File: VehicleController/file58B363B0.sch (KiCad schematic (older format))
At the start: 4 parts

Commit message: Added GPS, DAC, Isolation sheet, buzzer to VC
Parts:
- added C?: C_Small, symbol C_Small
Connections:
- wire segments 23 -> 27
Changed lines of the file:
@@
 $Descr A4 11693 8268
 encoding utf-8
-Sheet 4 4
+Sheet 4 5
 Title ""
 Date ""
@@
 	6900 3150 7050 3150
 Wire Wire Line
-	7050 3150 7050 3350
+	7050 3150 7050 3250
+Wire Wire Line
+	7050 3250 7050 3350
 Wire Wire Line
 	6900 3250 7050 3250
 Wire Wire Line
-	6250 2900 6250 3050
+	6250 2900 6250 2950
+Wire Wire Line
+	6250 2950 6250 3050
 Wire Wire Line
 	6400 2950 6250 2950
@@
 Text Label 7200 3050 2    60   ~ 0
 CANL
+$Comp
+L C_Small C?
+U 1 1 58B0DDAC
+P 5250 3950
+F 0 "C?" H 5342 3996 50  0000 L CNN
+F 1 "C_Small" H 5342 3905 50  0000 L CNN
+F 2 "" H 5250 3950 50  0000 C CNN
+F 3 "" H 5250 3950 50  0000 C CNN
+	1    5250 3950
+	-1   0    0    -1
+$EndComp
+$Comp
+L +5V #PWR?
+U 1 1 58B0DEC8
+P 5250 3750
+F 0 "#PWR?" H 5250 3600 50  0001 C CNN
+F 1 "+5V" H 5265 3923 50  0000 C CNN
+F 2 "" H 5250 3750 50  0000 C CNN
+F 3 "" H 5250 3750 50  0000 C CNN
+	1    5250 3750
+	1    0    0    -1
+$EndComp
+Wire Wire Line
+	5250 3850 5250 3750
+$Comp
+L GND #PWR?
+U 1 1 58B0DF2A
+P 5250 4200
+F 0 "#PWR?" H 5250 3950 50  0001 C CNN
+F 1 "GND" H 5255 4027 50  0000 C CNN
+F 2 "" H 5250 4200 50  0000 C CNN
+F 3 "" H 5250 4200 50  0000 C CNN
+	1    5250 4200
+	1    0    0    -1
+$EndComp
+Wire Wire Line
+	5250 4200 5250 4050
 $EndSCHEMATC

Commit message: 3D model of 16 pin, MX150_8 pin symbol
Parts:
- removed P?: CAN_MX150, symbol CONN_02X04
- added P?: MX150_8, symbol MX150_8
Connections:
- net labels removed: +12V
- wire segments 27 -> 15
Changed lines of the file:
@@
 $EndDescr
-$Comp
-L CONN_02X04 P?
-U 1 1 58B3656F
-P 6650 3100
-F 0 "P?" H 6650 3465 50  0000 C CNN
-F 1 "CAN_MX150" H 6650 3374 50  0000 C CNN
-F 2 "" H 6650 1900 50  0000 C CNN
-F 3 "" H 6650 1900 50  0000 C CNN
-	1    6650 3100
-	1    0    0    -1
-$EndComp
-$Comp
-L +12V #PWR?
-U 1 1 58B36576
-P 6250 2900
-F 0 "#PWR?" H 6250 2750 50  0001 C CNN
-F 1 "+12V" H 6265 3073 50  0000 C CNN
-F 2 "" H 6250 2900 50  0000 C CNN
-F 3 "" H 6250 2900 50  0000 C CNN
-	1    6250 2900
-	-1   0    0    -1
-$EndComp
-$Comp
-L GND #PWR?
-U 1 1 58B3657C
-P 7050 3350
-F 0 "#PWR?" H 7050 3100 50  0001 C CNN
-F 1 "GND" H 7055 3177 50  0000 C CNN
-F 2 "" H 7050 3350 50  0000 C CNN
-F 3 "" H 7050 3350 50  0000 C CNN
-	1    7050 3350
-	1    0    0    -1
-$EndComp
-Text Label 6100 3150 0    60   ~ 0
-CANH
-Text Label 6100 3250 0    60   ~ 0
-CANL
 $Comp
 L MCP2551 U?
@@
 Text Label 5900 2500 2    60   ~ 0
 CANH
-Wire Wire Line
-	6900 2950 7200 2950
-Wire Wire Line
-	6900 3050 7200 3050
-Connection ~ 6250 2950
-Wire Wire Line
-	6250 3050 6400 3050
-Connection ~ 7050 3250
-Wire Wire Line
-	6900 3150 7050 3150
-Wire Wire Line
-	7050 3150 7050 3250
-Wire Wire Line
-	7050 3250 7050 3350
-Wire Wire Line
-	6900 3250 7050 3250
-Wire Wire Line
-	6250 2900 6250 2950
-Wire Wire Line
-	6250 2950 6250 3050
-Wire Wire Line
-	6400 2950 6250 2950
-Wire Wire Line
-	5850 3250 6400 3250
-Wire Wire Line
-	5850 3150 6400 3150
+Text HLabel 4700 3150 0    60   Input ~ 0
+CANTX
+Text HLabel 4700 3250 0    60   Input ~ 0
+CANRX
+$Comp
+L C_Small C?
+U 1 1 58B0DDAC
+P 5250 3950
+F 0 "C?" H 5342 3996 50  0000 L CNN
+F 1 "C_Small" H 5342 3905 50  0000 L CNN
+F 2 "" H 5250 3950 50  0000 C CNN
+F 3 "" H 5250 3950 50  0000 C CNN
+	1    5250 3950
+	-1   0    0    -1
+$EndComp
+$Comp
+L +5V #PWR?
+U 1 1 58B0DEC8
+P 5250 3750
+F 0 "#PWR?" H 5250 3600 50  0001 C CNN
+F 1 "+5V" H 5265 3923 50  0000 C CNN
+F 2 "" H 5250 3750 50  0000 C CNN
+F 3 "" H 5250 3750 50  0000 C CNN
+	1    5250 3750
+	1    0    0    -1
+$EndComp
+$Comp
+L GND #PWR?
+U 1 1 58B0DF2A
+P 5250 4200
+F 0 "#PWR?" H 5250 3950 50  0001 C CNN
+F 1 "GND" H 5255 4027 50  0000 C CNN
+F 2 "" H 5250 4200 50  0000 C CNN
+F 3 "" H 5250 4200 50  0000 C CNN
+	1    5250 4200
+	1    0    0    -1
+$EndComp
 Wire Wire Line
 	5850 3350 5950 3350
@@
 Wire Wire Line
 	5600 2500 5900 2500
-Text HLabel 4700 3150 0    60   Input ~ 0
-CANTX
-Text HLabel 4700 3250 0    60   Input ~ 0
-CANRX
-Text Label 7200 2950 2    60   ~ 0
-CANH
-Text Label 7200 3050 2    60   ~ 0
-CANL
+Wire Wire Line
+	5250 3850 5250 3750
+Wire Wire Line
+	5250 4200 5250 4050
 $Comp
-L C_Small C?
-U 1 1 58B0DDAC
-P 5250 3950
-F 0 "C?" H 5342 3996 50  0000 L CNN
-F 1 "C_Small" H 5342 3905 50  0000 L CNN
-F 2 "" H 5250 3950 50  0000 C CNN
-F 3 "" H 5250 3950 50  0000 C CNN
-	1    5250 3950
-	-1   0    0    -1
-$EndComp
-$Comp
-L +5V #PWR?
-U 1 1 58B0DEC8
-P 5250 3750
-F 0 "#PWR?" H 5250 3600 50  0001 C CNN
-F 1 "+5V" H 5265 3923 50  0000 C CNN
-F 2 "" H 5250 3750 50  0000 C CNN
-F 3 "" H 5250 3750 50  0000 C CNN
-	1    5250 3750
+L MX150_8 P?
+U 1 1 58B7A4A8
+P 6650 3100
+F 0 "P?" H 6650 3465 50  0000 C CNN
+F 1 "MX150_8" H 6650 3374 50  0000 C CNN
+F 2 "" H 6650 1900 50  0000 C CNN
+F 3 "" H 6650 1900 50  0000 C CNN
+	1    6650 3100
 	1    0    0    -1
 $EndComp
-Wire Wire Line
-	5250 3850 5250 3750
-$Comp
-L GND #PWR?
-U 1 1 58B0DF2A
-P 5250 4200
-F 0 "#PWR?" H 5250 3950 50  0001 C CNN
-F 1 "GND" H 5255 4027 50  0000 C CNN
-F 2 "" H 5250 4200 50  0000 C CNN
-F 3 "" H 5250 4200 50  0000 C CNN
-	1    5250 4200
-	1    0    0    -1
-$EndComp
-Wire Wire Line
-	5250 4200 5250 4050
 $EndSCHEMATC

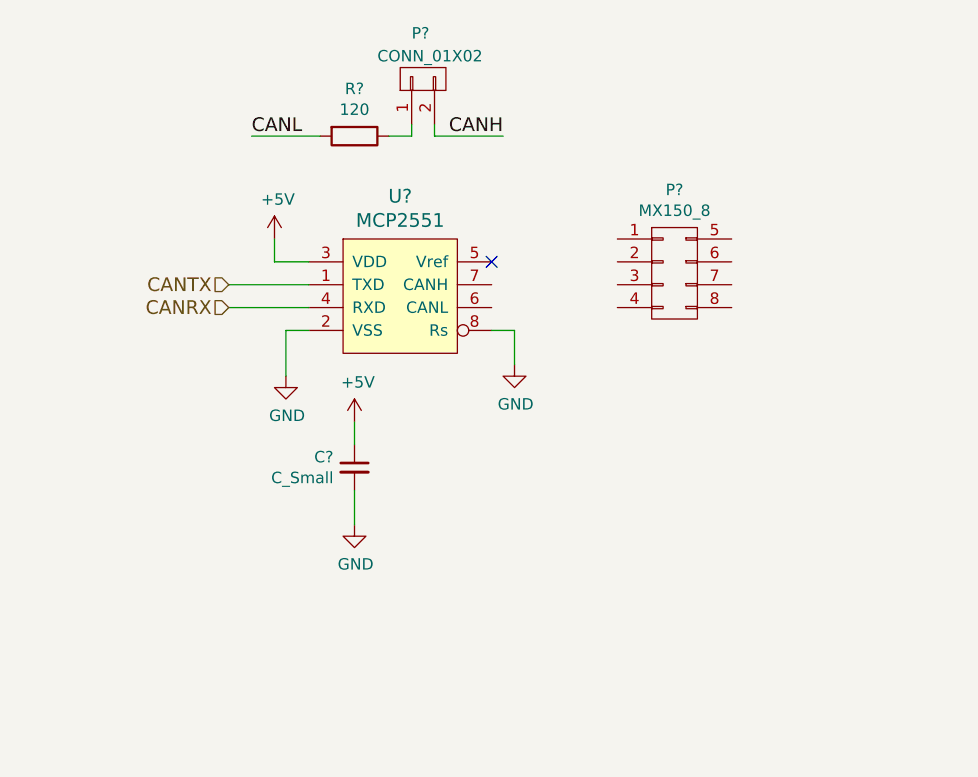
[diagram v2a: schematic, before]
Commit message: Add MX150 8 pin, add Motor Controller connector
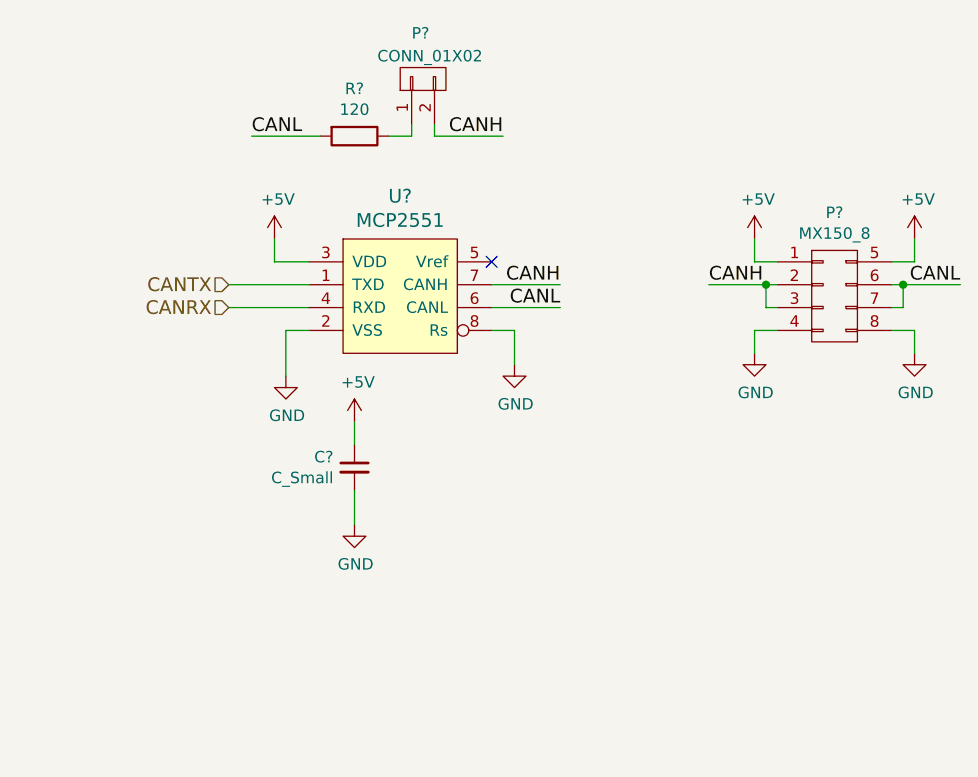
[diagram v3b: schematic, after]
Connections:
- net +5V: now also P?.1 (P1), P?.5 (P2)
- net CANH: now also P?.2 (P3), P?.3 (P5), U?.7 (CANH)
- net CANL: now also P?.6 (P4), P?.7 (P6), U?.6 (CANL)
- net GND: now also P?.4 (P7), P?.8 (P8)
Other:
- moved on the sheet: P?
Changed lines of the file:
@@
 LIBS:relays
 LIBS:SystemBlocks
+LIBS:dc-dc
+LIBS:Power_Management
 LIBS:VehicleController-cache
 EELAYER 26 0
@@
 L MX150_8 P?
 U 1 1 58B7A4A8
-P 6650 3100
-F 0 "P?" H 6650 3465 50  0000 C CNN
-F 1 "MX150_8" H 6650 3374 50  0000 C CNN
-F 2 "" H 6650 1900 50  0000 C CNN
-F 3 "" H 6650 1900 50  0000 C CNN
-	1    6650 3100
-	1    0    0    -1
-$EndComp
+P 7350 3200
+F 0 "P?" H 7350 3565 50  0000 C CNN
+F 1 "MX150_8" H 7350 3474 50  0000 C CNN
+F 2 "" H 7350 2000 50  0000 C CNN
+F 3 "" H 7350 2000 50  0000 C CNN
+	1    7350 3200
+	1    0    0    -1
+$EndComp
+Wire Wire Line
+	5850 3150 6150 3150
+Text Label 6150 3150 2    60   ~ 0
+CANH
+Text Label 6150 3250 2    60   ~ 0
+CANL
+Wire Wire Line
+	5850 3250 6150 3250
+Text Label 6800 3150 0    60   ~ 0
+CANH
+Wire Wire Line
+	6800 3150 7100 3150
+Wire Wire Line
+	7100 3250 7050 3250
+Wire Wire Line
+	7050 3250 7050 3150
+Connection ~ 7050 3150
+$Comp
+L +5V #PWR?
+U 1 1 58B7F5CF
+P 7000 2950
+F 0 "#PWR?" H 7000 2800 50  0001 C CNN
+F 1 "+5V" H 7015 3123 50  0000 C CNN
+F 2 "" H 7000 2950 50  0000 C CNN
+F 3 "" H 7000 2950 50  0000 C CNN
+	1    7000 2950
+	1    0    0    -1
+$EndComp
+Wire Wire Line
+	7000 2950 7000 3050
+Wire Wire Line
+	7000 3050 7100 3050
+$Comp
+L GND #PWR?
+U 1 1 58B7F609
+P 7000 3450
+F 0 "#PWR?" H 7000 3200 50  0001 C CNN
+F 1 "GND" H 7005 3277 50  0000 C CNN
+F 2 "" H 7000 3450 50  0000 C CNN
+F 3 "" H 7000 3450 50  0000 C CNN
+	1    7000 3450
+	1    0    0    -1
+$EndComp
+Wire Wire Line
+	7000 3450 7000 3350
+Wire Wire Line
+	7000 3350 7100 3350
+Wire Wire Line
+	7600 3150 7900 3150
+Text Label 7900 3150 2    60   ~ 0
+CANL
+Wire Wire Line
+	7600 3250 7650 3250
+Wire Wire Line
+	7650 3250 7650 3150
+Connection ~ 7650 3150
+$Comp
+L +5V #PWR?
+U 1 1 58B7F9CA
+P 7700 2950
+F 0 "#PWR?" H 7700 2800 50  0001 C CNN
+F 1 "+5V" H 7715 3123 50  0000 C CNN
+F 2 "" H 7700 2950 50  0000 C CNN
+F 3 "" H 7700 2950 50  0000 C CNN
+	1    7700 2950
+	1    0    0    -1
+$EndComp
+Wire Wire Line
+	7600 3050 7700 3050
+Wire Wire Line
+	7700 3050 7700 2950
+$Comp
+L GND #PWR?
+U 1 1 58B7FA08
+P 7700 3450
+F 0 "#PWR?" H 7700 3200 50  0001 C CNN
+F 1 "GND" H 7705 3277 50  0000 C CNN
+F 2 "" H 7700 3450 50  0000 C CNN
+F 3 "" H 7700 3450 50  0000 C CNN
+	1    7700 3450
+	1    0    0    -1
+$EndComp
+Wire Wire Line
+	7600 3350 7700 3350
+Wire Wire Line
+	7700 3350 7700 3450
 $EndSCHEMATC

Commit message: Add High-G Accel, connectors
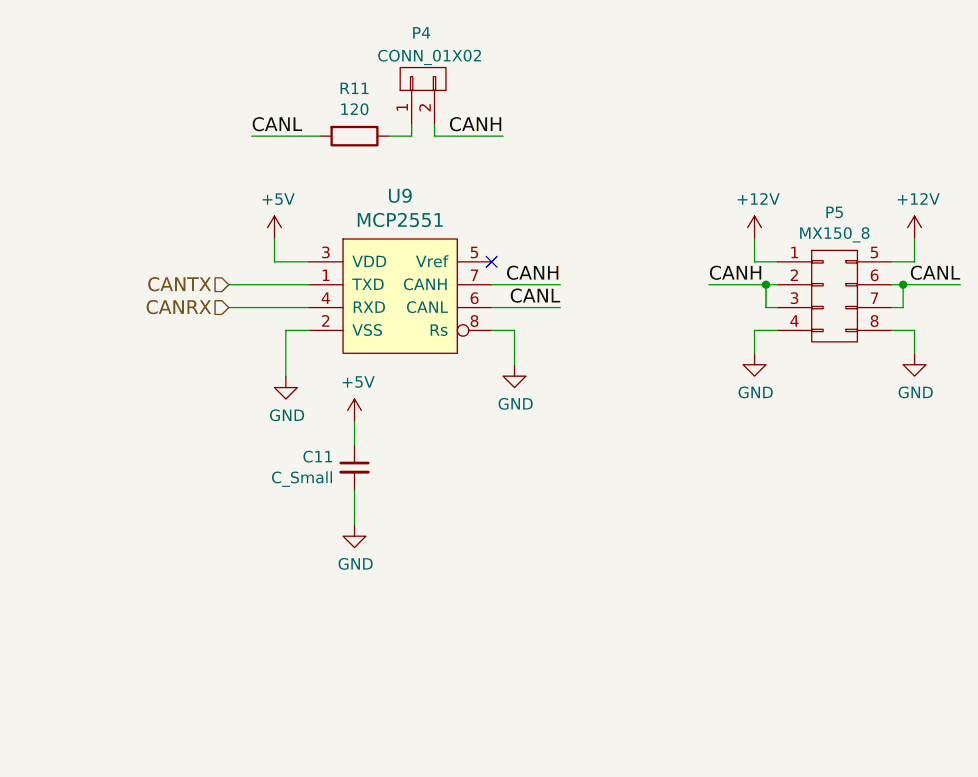
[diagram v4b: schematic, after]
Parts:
- gave numbers to parts that had none: 5
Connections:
- net +5V: no longer P5.1 (P1), P5.5 (P2)
- new net +12V: P5.1 (P1), P5.5 (P2)
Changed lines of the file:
@@
 LIBS:dc-dc
 LIBS:Power_Management
+LIBS:switches
 LIBS:VehicleController-cache
 EELAYER 26 0
@@
 $EndDescr
 $Comp
-L MCP2551 U?
+L MCP2551 U9
 U 1 1 58B36586
 P 5450 3250
-F 0 "U?" H 5450 3737 60  0000 C CNN
+F 0 "U9" H 5450 3737 60  0000 C CNN
 F 1 "MCP2551" H 5450 3631 60  0000 C CNN
 F 2 "" H 5450 3250 60  0000 C CNN
@@
 $EndComp
 $Comp
-L GND #PWR?
+L GND #PWR39
 U 1 1 58B3658D
 P 5950 3500
-F 0 "#PWR?" H 5950 3250 50  0001 C CNN
+F 0 "#PWR39" H 5950 3250 50  0001 C CNN
 F 1 "GND" H 5955 3327 50  0000 C CNN
 F 2 "" H 5950 3500 50  0000 C CNN
@@
 NoConn ~ 5850 3050
 $Comp
-L +5V #PWR?
+L +5V #PWR35
 U 1 1 58B36594
 P 4900 2950
-F 0 "#PWR?" H 4900 2800 50  0001 C CNN
+F 0 "#PWR35" H 4900 2800 50  0001 C CNN
 F 1 "+5V" H 4915 3123 50  0000 C CNN
 F 2 "" H 4900 2950 50  0000 C CNN
@@
 $EndComp
 $Comp
-L GND #PWR?
+L GND #PWR36
 U 1 1 58B3659A
 P 4950 3550
-F 0 "#PWR?" H 4950 3300 50  0001 C CNN
+F 0 "#PWR36" H 4950 3300 50  0001 C CNN
 F 1 "GND" H 4955 3377 50  0000 C CNN
 F 2 "" H 4950 3550 50  0000 C CNN
@@
 $EndComp
 $Comp
-L R R?
+L R R11
 U 1 1 58B365A2
 P 5250 2500
-F 0 "R?" V 5043 2500 50  0000 C CNN
+F 0 "R11" V 5043 2500 50  0000 C CNN
 F 1 "120" V 5134 2500 50  0000 C CNN
 F 2 "" V 5180 2500 50  0000 C CNN
@@
 CANL
 $Comp
-L CONN_01X02 P?
+L CONN_01X02 P4
 U 1 1 58B365AA
 P 5550 2250
-F 0 "P?" V 5750 2300 50  0000 R CNN
+F 0 "P4" V 5750 2300 50  0000 R CNN
 F 1 "CONN_01X02" V 5650 2450 50  0000 R CNN
 F 2 "" H 5550 2250 50  0000 C CNN
@@
 CANRX
 $Comp
-L C_Small C?
+L C_Small C11
 U 1 1 58B0DDAC
 P 5250 3950
-F 0 "C?" H 5342 3996 50  0000 L CNN
+F 0 "C11" H 5342 3996 50  0000 L CNN
 F 1 "C_Small" H 5342 3905 50  0000 L CNN
 F 2 "" H 5250 3950 50  0000 C CNN
@@
 $EndComp
 $Comp
-L +5V #PWR?
+L +5V #PWR37
 U 1 1 58B0DEC8
 P 5250 3750
-F 0 "#PWR?" H 5250 3600 50  0001 C CNN
+F 0 "#PWR37" H 5250 3600 50  0001 C CNN
 F 1 "+5V" H 5265 3923 50  0000 C CNN
 F 2 "" H 5250 3750 50  0000 C CNN
@@
 $EndComp
 $Comp
-L GND #PWR?
+L GND #PWR38
 U 1 1 58B0DF2A
 P 5250 4200
-F 0 "#PWR?" H 5250 3950 50  0001 C CNN
+F 0 "#PWR38" H 5250 3950 50  0001 C CNN
 F 1 "GND" H 5255 4027 50  0000 C CNN
 F 2 "" H 5250 4200 50  0000 C CNN
@@
 	5250 4200 5250 4050
 $Comp
-L MX150_8 P?
+L MX150_8 P5
 U 1 1 58B7A4A8
 P 7350 3200
-F 0 "P?" H 7350 3565 50  0000 C CNN
+F 0 "P5" H 7350 3565 50  0000 C CNN
 F 1 "MX150_8" H 7350 3474 50  0000 C CNN
 F 2 "" H 7350 2000 50  0000 C CNN
@@
 	7050 3250 7050 3150
 Connection ~ 7050 3150
-$Comp
-L +5V #PWR?
-U 1 1 58B7F5CF
-P 7000 2950
-F 0 "#PWR?" H 7000 2800 50  0001 C CNN
-F 1 "+5V" H 7015 3123 50  0000 C CNN
-F 2 "" H 7000 2950 50  0000 C CNN
-F 3 "" H 7000 2950 50  0000 C CNN
-	1    7000 2950
-	1    0    0    -1
-$EndComp
 Wire Wire Line
 	7000 2950 7000 3050
@@
 	7000 3050 7100 3050
 $Comp
-L GND #PWR?
+L GND #PWR41
 U 1 1 58B7F609
 P 7000 3450
-F 0 "#PWR?" H 7000 3200 50  0001 C CNN
+F 0 "#PWR41" H 7000 3200 50  0001 C CNN
 F 1 "GND" H 7005 3277 50  0000 C CNN
 F 2 "" H 7000 3450 50  0000 C CNN
@@
 	7650 3250 7650 3150
 Connection ~ 7650 3150
-$Comp
-L +5V #PWR?
-U 1 1 58B7F9CA
-P 7700 2950
-F 0 "#PWR?" H 7700 2800 50  0001 C CNN
-F 1 "+5V" H 7715 3123 50  0000 C CNN
-F 2 "" H 7700 2950 50  0000 C CNN
-F 3 "" H 7700 2950 50  0000 C CNN
-	1    7700 2950
-	1    0    0    -1
-$EndComp
 Wire Wire Line
 	7600 3050 7700 3050
@@
 	7700 3050 7700 2950
 $Comp
-L GND #PWR?
+L GND #PWR43
 U 1 1 58B7FA08
 P 7700 3450
-F 0 "#PWR?" H 7700 3200 50  0001 C CNN
+F 0 "#PWR43" H 7700 3200 50  0001 C CNN
 F 1 "GND" H 7705 3277 50  0000 C CNN
 F 2 "" H 7700 3450 50  0000 C CNN
@@
 Wire Wire Line
 	7700 3350 7700 3450
+$Comp
+L +12V #PWR40
+U 1 1 58BABA64
+P 7000 2950
+F 0 "#PWR40" H 7000 2800 50  0001 C CNN
+F 1 "+12V" H 7015 3123 50  0000 C CNN
+F 2 "" H 7000 2950 50  0000 C CNN
+F 3 "" H 7000 2950 50  0000 C CNN
+	1    7000 2950
+	1    0    0    -1
+$EndComp
+$Comp
+L +12V #PWR42
+U 1 1 58BABA85
+P 7700 2950
+F 0 "#PWR42" H 7700 2800 50  0001 C CNN
+F 1 "+12V" H 7715 3123 50  0000 C CNN
+F 2 "" H 7700 2950 50  0000 C CNN
+F 3 "" H 7700 2950 50  0000 C CNN
+	1    7700 2950
+	1    0    0    -1
+$EndComp
 $EndSCHEMATC
